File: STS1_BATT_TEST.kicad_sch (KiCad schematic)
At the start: 6 parts, among them J1 TE 282834-6, J2 Conn_01x15

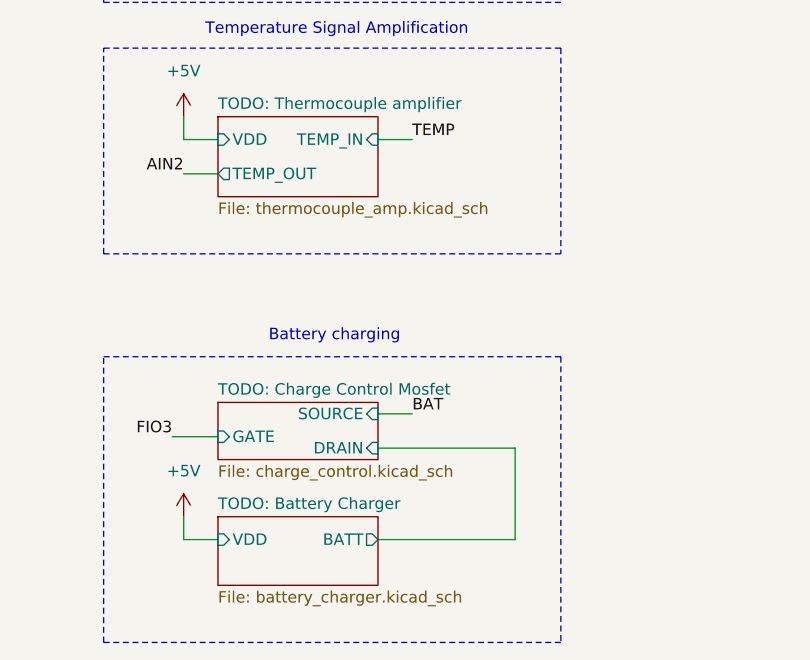
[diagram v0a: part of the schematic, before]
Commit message: Added discharge Mosfet.
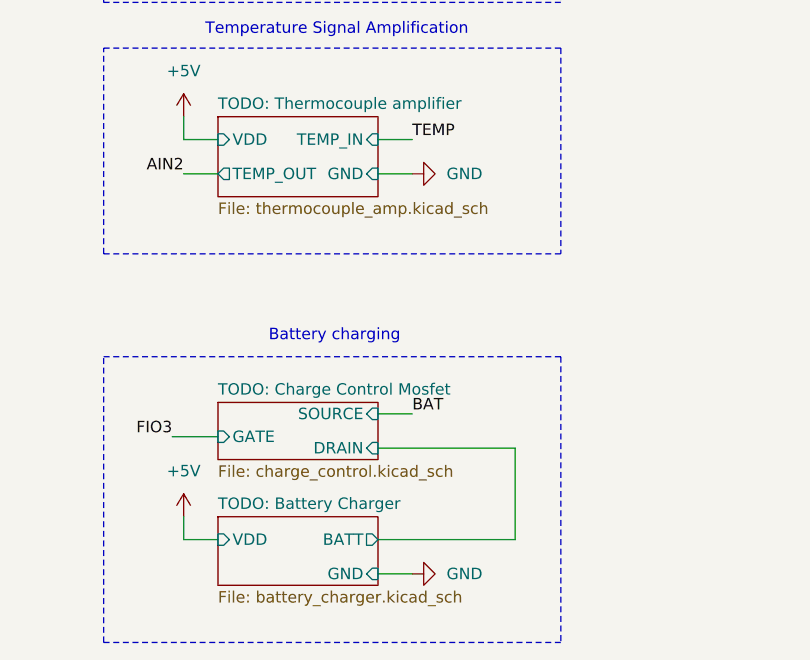
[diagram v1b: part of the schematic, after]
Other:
- sheet TODO: Battery Charger ports: added GND; removed none
- sheet TODO: Thermocouple amplifier ports: added GND; removed none
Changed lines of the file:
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@@
+	(wire
+		(pts
+			(xy 151.13 99.06) (xy 154.94 99.06)
+		)
+		(stroke
+			(width 0)
+			(type default)
+		)
+	)
 	(wire
 		(pts
@@
 		(pts
 			(xy 38.1 73.66) (xy 38.1 76.2)
+		)
+		(stroke
+			(width 0)
+			(type default)
+		)
+	)
+	(wire
+		(pts
+			(xy 151.13 143.51) (xy 154.94 143.51)
 		)
 		(stroke
@@
 				(path "/3a2a22aa-6e8a-41f2-9388-8b5b5cbcd4ba"
 					(reference "#PWR02")
+					(unit 1)
+				)
+			)
+		)
+	)
+	(symbol
+		(lib_id "power:GND")
+		(at 154.94 143.51 90)
+		(unit 1)
+		(exclude_from_sim no)
+		(in_bom yes)
+		(on_board yes)
+		(dnp no)
+		(fields_autoplaced yes)
+		(property "Reference" "#PWR08"
+			(at 161.29 143.51 0)
+			(effects
+				(font
+					(size 1.27 1.27)
+				)
+				(hide yes)
+			)
+		)
+		(property "Value" "GND"
+			(at 158.75 143.5099 90)
+			(effects
+				(font
+					(size 1.27 1.27)
+				)
+				(justify right)
+			)
+		)
+		(property "Footprint" ""
+			(at 154.94 143.51 0)
+			(effects
+				(font
+					(size 1.27 1.27)
+				)
+				(hide yes)
+			)
+		)
+		(property "Datasheet" ""
+			(at 154.94 143.51 0)
+			(effects
+				(font
+					(size 1.27 1.27)
+				)
+				(hide yes)
+			)
+		)
+		(property "Description" "Power symbol creates a global label with name \"GND\" , ground"
+			(at 154.94 143.51 0)
+			(effects
+				(font
+					(size 1.27 1.27)
+				)
+				(hide yes)
+			)
+		)
+		(pin "1"
+		)
+		(instances
+			(project "STS1_BATT_TEST"
+				(path "/3a2a22aa-6e8a-41f2-9388-8b5b5cbcd4ba"
+					(reference "#PWR08")
+					(unit 1)
+				)
+			)
+		)
+	)
+	(symbol
+		(lib_id "power:GND")
+		(at 154.94 99.06 90)
+		(unit 1)
+		(exclude_from_sim no)
+		(in_bom yes)
+		(on_board yes)
+		(dnp no)
+		(fields_autoplaced yes)
+		(property "Reference" "#PWR07"
+			(at 161.29 99.06 0)
+			(effects
+				(font
+					(size 1.27 1.27)
+				)
+				(hide yes)
+			)
+		)
+		(property "Value" "GND"
+			(at 158.75 99.0599 90)
+			(effects
+				(font
+					(size 1.27 1.27)
+				)
+				(justify right)
+			)
+		)
+		(property "Footprint" ""
+			(at 154.94 99.06 0)
+			(effects
+				(font
+					(size 1.27 1.27)
+				)
+				(hide yes)
+			)
+		)
+		(property "Datasheet" ""
+			(at 154.94 99.06 0)
+			(effects
+				(font
+					(size 1.27 1.27)
+				)
+				(hide yes)
+			)
+		)
+		(property "Description" "Power symbol creates a global label with name \"GND\" , ground"
+			(at 154.94 99.06 0)
+			(effects
+				(font
+					(size 1.27 1.27)
+				)
+				(hide yes)
+			)
+		)
+		(pin "1"
+		)
+		(instances
+			(project "STS1_BATT_TEST"
+				(path "/3a2a22aa-6e8a-41f2-9388-8b5b5cbcd4ba"
+					(reference "#PWR07")
 					(unit 1)
 				)
@@
 			)
 		)
+		(pin "GND" input
+			(at 151.13 99.06 0)
+			(effects
+				(font
+					(size 1.27 1.27)
+				)
+				(justify right)
+			)
+		)
 		(instances
 			(project "STS1_BATT_TEST"
@@
 			(effects
 				(font
+					(size 1.27 1.27)
+				)
+				(justify right)
+			)
+		)
+		(pin "GND" input
+			(at 151.13 143.51 0)
+			(effects
+				(font

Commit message: Prepared STS1_BATT_TEST.
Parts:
- added J4: Conn_01x04, STS1_Connectors:TE_282834-4, symbol Connector_Generic:Conn_01x04
- added U1: TC4420VOA713, Package_SO:SOIC-8_5.275x5.275mm_P1.27mm, symbol STS_Transistor_FET:TC4420
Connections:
- net BAT is gone; now on net AIN0: J2.1 (Pin_1), J2.2 (Pin_2), J2.3 (Pin_3), J2.4 (Pin_4), J2.5 (Pin_5), J2.6 (Pin_6), J2.7 (Pin_7)
- net +5V: now also U1.1 (VDD), U1.8 (VDD)
- net AIN0: now also J4.1 (Pin_1)
- net FIO0: now also U1.2 (Input)
- net GND: now also J4.3 (Pin_3), J4.4 (Pin_4), U1.4 (GND), U1.5 (GND)
- net TEMP: now also J4.2 (Pin_2)
- new net Load Mosfet with cooling/GATE: U1.6 (Output), U1.7 (Output)
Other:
- sheet TODO: Load Mosfet with cooling renamed Load Mosfet with cooling
- removed sheet TODO: Charge Control Mosfet
- sheet TODO: Battery Charger ports: added ENABLE; removed none
- note added: "AIN0 ... Battery voltage AIN1 ... Voltage after shunt AIN2 ... Temperature reading FIO0 ... Load mosfet control FIO3 ... Charging control"
- note added: "Secondary screw terminal connector"
- moved on the sheet: J2
